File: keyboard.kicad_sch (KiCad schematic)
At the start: 352 parts, among them J1 USB_B_Micro, J2 Conn_01x06, J3 USB_C_Receptacle_USB2.0, K0 KEYSW, K1 KEYSW, K10 KEYSW, K100 KEYSW, K101 KEYSW, K102 KEYSW, K103 KEYSW, K104 KEYSW, K105 KEYSW, K106 KEYSW, K107 KEYSW, K108 KEYSW, K11 KEYSW, K12 KEYSW, K13 KEYSW, K14 KEYSW, K15 KEYSW, K16 KEYSW, K17 KEYSW, K18 KEYSW, K19 KEYSW, K2 KEYSW, K20 KEYSW, K21 KEYSW, K22 KEYSW, K23 KEYSW, K24 KEYSW, K25 KEYSW, K26 KEYSW, K27 KEYSW, K28 KEYSW, K29 KEYSW, K3 KEYSW, K30 KEYSW, K31 KEYSW, K32 KEYSW, K33 KEYSW, K34 KEYSW, K35 KEYSW, K36 KEYSW, K37 KEYSW, K38 KEYSW, K39 KEYSW, K4 KEYSW, K40 KEYSW, K41 KEYSW, K42 KEYSW, K43 KEYSW, K44 KEYSW, K45 KEYSW, K46 KEYSW, K47 KEYSW, K48 KEYSW, K49 KEYSW, K5 KEYSW, K50 KEYSW, K51 KEYSW, K52 KEYSW, K53 KEYSW, K54 KEYSW, K55 KEYSW, K56 KEYSW, K57 KEYSW, K58 KEYSW, K59 KEYSW, K6 KEYSW, K60 KEYSW, K61 KEYSW, K62 KEYSW, K63 KEYSW, K64 KEYSW, K65 KEYSW, K66 KEYSW, K67 KEYSW, K68 KEYSW, K69 KEYSW, K7 KEYSW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

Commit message: leds 1
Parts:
- renumbered D109 to D200, D123 to D201, D130 to D202, D135 to D203, D140 to D204, D148 to D205, D154 to D206, D159 to D207, D164 to D208, D171 to D209, D178 to D210, D182 to D211, D186 to D212, D199 to D213, D210 to D214, D218 to D215, D187 to D216, D195 to D217, D206 to D218, D215 to D219, D113 to D220, D118 to D221, D124 to D222, D129 to D223, D134 to D224, D139 to D225, D144 to D226, D150 to D227, D155 to D228, D160 to D229, D166 to D230, D172 to D231, D177 to D232, D184 to D233, D196 to D234, D207 to D235, D216 to D236, D188 to D237, D197 to D238, D208 to D239, D217 to D240, D115 to D241, D120 to D242, D126 to D243, D131 to D244, D136 to D245, D141 to D246, D145 to D247, D151 to D248, D156 to D249, D161 to D250, D167 to D251, D173 to D252, D179 to D253, D185 to D254, D194 to D255, D203 to D256, D214 to D257, D190 to D258, D200 to D259, D211 to D260, D219 to D261, D117 to D262, D122 to D263, D128 to D264, D133 to D265, D138 to D266, D143 to D267, D147 to D268, D153 to D269, D158 to D270, D163 to D271, D169 to D272, D175 to D273, D180 to D274

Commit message: pcb almost done
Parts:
- removed J1: USB_B_Micro, Connector_USB:USB_Micro-B_Wuerth_629105150521_CircularHoles, symbol Connector:USB_B_Micro
- added C9: 0.1u, Capacitor_SMD:C_0805_2012Metric_Pad1.15x1.40mm_HandSolder, symbol Device:C
- added F1: Fuse, Fuse:Fuse_1206_3216Metric_Pad1.42x1.75mm_HandSolder, symbol Device:Fuse
- added JP3: Jumper_2_Open, Jumper:SolderJumper-2_P1.3mm_Open_Pad1.0x1.5mm, symbol Jumper:Jumper_2_Open
- added JP4: SolderJumper_3_Open, Jumper:SolderJumper-3_P1.3mm_Open_RoundedPad1.0x1.5mm, symbol Jumper:SolderJumper_3_Open
- added Q1: Q_PMOS_DGS, Package_TO_SOT_SMD:ATPAK-2, symbol Device:Q_PMOS_DSG
- added Q2: Q_NMOS_DGS, Package_TO_SOT_SMD:SOT-23, symbol Device:Q_NMOS_DSG
- added R1, R4: 5.11k, Resistor_SMD:R_0805_2012Metric_Pad1.20x1.40mm_HandSolder, symbol Device:R
- added R5: 1M, Resistor_SMD:R_0805_2012Metric_Pad1.20x1.40mm_HandSolder, symbol Device:R
- added R6: 10k, Resistor_SMD:R_0805_2012Metric_Pad1.20x1.40mm_HandSolder, symbol Device:R
- added R7: 220k, Resistor_SMD:R_0805_2012Metric_Pad1.20x1.40mm_HandSolder, symbol Device:R
- added X1: ASE-xxxMHz, Oscillator:Oscillator_SMD_Abracon_ASE-4Pin_3.2x2.5mm, symbol Oscillator:ASE-xxxMHz
- C6, C7, C8: footprint Capacitor_SMD:C_0805_2012Metric_Pad1.15x1.40mm_HandSolder -> Capacitor_SMD:C_0805_2012Metric_Pad1.18x1.45mm_HandSolder
- J2: footprint Connector_PinHeader_2.54mm:PinHeader_1x06_P2.54mm_Vertical -> Connector_PinHeader_1.27mm:PinHeader_1x06_P1.27mm_Vertical
- J3: footprint (none) -> Connector_USB:USB_C_Receptacle_GCT_USB4085
- renumbered D189 to D275, D198 to D276, D209 to D277, D116 to D278, D121 to D279, D127 to D280, D132 to D281, D137 to D282, D142 to D283, D146 to D284, D152 to D285, D157 to D286, D162 to D287, D168 to D288, D174 to D289, D181 to D290, D205 to D291, D191 to D292, D201 to D293, D212 to D294, D220 to D295, D114 to D296, D119 to D297, D125 to D298, D149 to D299, D165 to D300, D170 to D301, D176 to D302, D183 to D303, D193 to D304, D202 to D305, D213 to D306, D192 to D307, D204 to D308
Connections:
- net Col_0: now also U1.20 (PA4); no longer U1.4 (PC15)
- net Col_1: now also U1.21 (PA5); no longer U1.3 (PC14)
- net GND: now also D110.2 (VSS), D111.2 (VSS), D112.2 (VSS), D200.2 (VSS), D201.2 (VSS), D202.2 (VSS), D203.2 (VSS), D204.2 (VSS), D205.2 (VSS), D206.2 (VSS), D207.2 (VSS), D208.2 (VSS), D209.2 (VSS), D210.2 (VSS), D211.2 (VSS), D212.2 (VSS), D213.2 (VSS), D214.2 (VSS), D215.2 (VSS), D216.2 (VSS), D217.2 (VSS), D218.2 (VSS), D219.2 (VSS), D220.2 (VSS), D221.2 (VSS), D222.2 (VSS), D223.2 (VSS), D224.2 (VSS), D225.2 (VSS), D226.2 (VSS), D227.2 (VSS), D228.2 (VSS), D229.2 (VSS), D230.2 (VSS), D231.2 (VSS), D232.2 (VSS), D233.2 (VSS), D234.2 (VSS), D235.2 (VSS), D236.2 (VSS), D237.2 (VSS), D238.2 (VSS), D239.2 (VSS), D240.2 (VSS), D241.2 (VSS), D242.2 (VSS), D243.2 (VSS), D244.2 (VSS), D245.2 (VSS), D246.2 (VSS), D247.2 (VSS), D248.2 (VSS), D249.2 (VSS), D250.2 (VSS), D251.2 (VSS), D252.2 (VSS), D253.2 (VSS), D254.2 (VSS), D255.2 (VSS), D256.2 (VSS), D257.2 (VSS), D258.2 (VSS), D259.2 (VSS), D260.2 (VSS), D261.2 (VSS), D262.2 (VSS), D263.2 (VSS), D264.2 (VSS), D265.2 (VSS), D266.2 (VSS), D267.2 (VSS), D268.2 (VSS), D269.2 (VSS), D270.2 (VSS), D271.2 (VSS), D272.2 (VSS), D273.2 (VSS), D274.2 (VSS), D275.2 (VSS), D276.2 (VSS), D277.2 (VSS), D278.2 (VSS), D279.2 (VSS), D280.2 (VSS), D281.2 (VSS), D282.2 (VSS), D283.2 (VSS), D284.2 (VSS), D285.2 (VSS), D286.2 (VSS), D287.2 (VSS), D288.2 (VSS), D289.2 (VSS), D290.2 (VSS), D291.2 (VSS), D292.2 (VSS), D293.2 (VSS), D294.2 (VSS), D295.2 (VSS), D296.2 (VSS), D297.2 (VSS), D298.2 (VSS), D299.2 (VSS), D300.2 (VSS), D301.2 (VSS), D302.2 (VSS), D303.2 (VSS), D304.2 (VSS), D305.2 (VSS), D306.2 (VSS), D307.2 (VSS), D308.2 (VSS), J3.A1 (GND), J3.A12 (GND), J3.B1 (GND), J3.B12 (GND), C9.2, JP4.3 (B), Q2.2 (S), R1.2, R4.2, R5.1, X1.2 (GND)
- net VBUS: now also J3.A4 (VBUS), J3.A9 (VBUS), J3.B4 (VBUS), J3.B9 (VBUS), F1.1
- net VCC: now also C9.1, JP4.1 (A), X1.4 (Vdd)
- net at R2.1: now also U1.44 (PA11); no longer U1.45 (PA12)
- net at R2.2: now also J3.A7 (D-), J3.B7 (D-)
- net at R3.1: now also U1.45 (PA12); no longer U1.44 (PA11)
- net at R3.2: now also J3.A6 (D+), J3.B6 (D+)
- net at D208.1 (DOUT): now also D209.3 (DIN)
- net at D208.3 (DIN): now also D207.1 (DOUT)
- net +5V: now reaches D208.4 (VDD)
- net +5V: now also D110.4 (VDD), D111.4 (VDD), D112.4 (VDD), D200.4 (VDD), D201.4 (VDD), D202.4 (VDD), D203.4 (VDD), D204.4 (VDD), D205.4 (VDD), D206.4 (VDD), D207.4 (VDD), D209.4 (VDD), D210.4 (VDD), D211.4 (VDD), D212.4 (VDD), D213.4 (VDD), D214.4 (VDD), D215.4 (VDD), D216.4 (VDD), D217.4 (VDD), D218.4 (VDD), D219.4 (VDD), D220.4 (VDD), D221.4 (VDD), D222.4 (VDD), D223.4 (VDD), D224.4 (VDD), D225.4 (VDD), D226.4 (VDD), D227.4 (VDD), D228.4 (VDD), D229.4 (VDD), D230.4 (VDD), D231.4 (VDD), D232.4 (VDD), D233.4 (VDD), D234.4 (VDD), D235.4 (VDD), D236.4 (VDD), D237.4 (VDD), D238.4 (VDD), D239.4 (VDD), D240.4 (VDD), D241.4 (VDD), D242.4 (VDD), D243.4 (VDD), D244.4 (VDD), D245.4 (VDD), D246.4 (VDD), D247.4 (VDD), D248.4 (VDD), D249.4 (VDD), D250.4 (VDD), D251.4 (VDD), D252.4 (VDD), D253.4 (VDD), D254.4 (VDD), D255.4 (VDD), D256.4 (VDD), D257.4 (VDD), D258.4 (VDD), D259.4 (VDD), D260.4 (VDD), D261.4 (VDD), D262.4 (VDD), D263.4 (VDD), D264.4 (VDD), D265.4 (VDD), D266.4 (VDD), D267.4 (VDD), D268.4 (VDD), D269.4 (VDD), D270.4 (VDD), D271.4 (VDD), D272.4 (VDD), D273.4 (VDD), D274.4 (VDD), D275.4 (VDD), D276.4 (VDD), D277.4 (VDD), D278.4 (VDD), D279.4 (VDD), D280.4 (VDD), D281.4 (VDD), D282.4 (VDD), D283.4 (VDD), D284.4 (VDD), D285.4 (VDD), D286.4 (VDD), D287.4 (VDD), D288.4 (VDD), D289.4 (VDD), D290.4 (VDD), D291.4 (VDD), D292.4 (VDD), D293.4 (VDD), D294.4 (VDD), D295.4 (VDD), D296.4 (VDD), D297.4 (VDD), D298.4 (VDD), D299.4 (VDD), D300.4 (VDD), D301.4 (VDD), D302.4 (VDD), D303.4 (VDD), D304.4 (VDD), D305.4 (VDD), D306.4 (VDD), D307.4 (VDD), D308.4 (VDD), JP3.1 (A), Q1.1 (D)
- net at D253.1 (DOUT): now also D254.3 (DIN)
- net at D253.3 (DIN): now also D252.1 (DOUT)
- net at D259.1 (DOUT): now also D260.3 (DIN)
- net at D259.3 (DIN): now also D258.1 (DOUT)
- net at D302.1 (DOUT): now also D301.3 (DIN)
- net at D302.3 (DIN): now also D303.1 (DOUT)
- net at D241.1 (DOUT): now also D242.3 (DIN)
- net at D241.3 (DIN): now also D220.1 (DOUT)
- net at D303.3 (DIN): now also D304.1 (DOUT)
- net at D256.1 (DOUT): now also D257.3 (DIN)
- net at D256.3 (DIN): now also D255.1 (DOUT)
- net at D267.1 (DOUT): now also D266.3 (DIN)
- net at D267.3 (DIN): now also D268.1 (DOUT)
- net at D301.1 (DOUT): now also D300.3 (DIN)
- net at D295.1 (DOUT): now also D308.3 (DIN)
- net at D295.3 (DIN): now also D294.1 (DOUT)
- net at D220.3 (DIN): now also D221.1 (DOUT)
- net at D299.1 (DOUT): now also D298.3 (DIN)
- net at D299.3 (DIN): now also D300.1 (DOUT)
- net at D110.1 (DOUT): now also D274.3 (DIN)
- net at D110.3 (DIN): now also D111.1 (DOUT)
- net at D269.1 (DOUT): now also D268.3 (DIN)
- net at D269.3 (DIN): now also D270.1 (DOUT)
- net at D255.3 (DIN): now also D254.1 (DOUT)
- net at D242.1 (DOUT): now also D243.3 (DIN)
- net at D262.1 (DOUT): now also D278.3 (DIN)
- net at D262.3 (DIN): now also D263.1 (DOUT)
- net at D205.1 (DOUT): now also D206.3 (DIN)
- net at D205.3 (DIN): now also D204.1 (DOUT)
- net at D280.1 (DOUT): now also D281.3 (DIN)
- net at D280.3 (DIN): now also D279.1 (DOUT)
- net at D239.1 (DOUT): now also D238.3 (DIN)
- net at D239.3 (DIN): now also D240.1 (DOUT)
- net at D305.1 (DOUT): now also D304.3 (DIN)
- net at D305.3 (DIN): now also D306.1 (DOUT)
- net at D224.1 (DOUT): now also D223.3 (DIN)
- net at D224.3 (DIN): now also D225.1 (DOUT)
- net at D237.1 (DOUT): now also D236.3 (DIN)
- net at D237.3 (DIN): now also D238.1 (DOUT)
- net at D216.1 (DOUT): now also D217.3 (DIN)
- net at D216.3 (DIN): now also D215.1 (DOUT)
- net at D229.1 (DOUT): now also D228.3 (DIN)
- net at D229.3 (DIN): now also D230.1 (DOUT)
- net at D293.1 (DOUT): now also D294.3 (DIN)
- net at D293.3 (DIN): now also D292.1 (DOUT)
- net at D289.1 (DOUT): now also D290.3 (DIN)
- net at D289.3 (DIN): now also D288.1 (DOUT)
- net at D281.1 (DOUT): now also D282.3 (DIN)
- net D_LED: now reaches U1.41 (PA8)
- net D_LED: now also D200.3 (DIN)
- net LED_EN: now reaches U1.61 (PB8)
- net LED_EN: now also R7.1
- net at D230.3 (DIN): now also D231.1 (DOUT)
- net at D286.1 (DOUT): now also D287.3 (DIN)
- net at D286.3 (DIN): now also D285.1 (DOUT)
- net at D235.1 (DOUT): now also D234.3 (DIN)
- net at D235.3 (DIN): now also D236.1 (DOUT)
- net at D243.1 (DOUT): now also D244.3 (DIN)
- net at D307.1 (DOUT): now also D306.3 (DIN)
- net at D307.3 (DIN): now also D308.1 (DOUT)
- net at D257.1 (DOUT): now also D258.3 (DIN)
- net at D225.3 (DIN): now also D226.1 (DOUT)
- net at D251.1 (DOUT): now also D252.3 (DIN)
- net at D251.3 (DIN): now also D250.1 (DOUT)
- net at D273.1 (DOUT): now also D272.3 (DIN)
- net at D273.3 (DIN): now also D274.1 (DOUT)
- net at D203.1 (DOUT): now also D204.3 (DIN)
- net at D203.3 (DIN): now also D202.1 (DOUT)
- net at D232.1 (DOUT): now also D231.3 (DIN)
- net at D232.3 (DIN): now also D233.1 (DOUT)
- net at D233.3 (DIN): now also D234.1 (DOUT)
- net at D275.1 (DOUT): now also D112.3 (DIN)
- net at D275.3 (DIN): now also D276.1 (DOUT)
- net at D284.1 (DOUT): now also D285.3 (DIN)
- net at D284.3 (DIN): now also D283.1 (DOUT)
- net at J3.A5 (CC1): now also R4.1
- net at J3.B5 (CC2): now also R1.1
- net at J3.S1 (SHIELD): now also R5.2
- net at D290.1 (DOUT): now also D291.3 (DIN)
- net at D297.1 (DOUT): now also D296.3 (DIN)
- net at D297.3 (DIN): now also D298.1 (DOUT)
- net at D282.1 (DOUT): now also D283.3 (DIN)
- net at D211.1 (DOUT): now also D212.3 (DIN)
- net at D211.3 (DIN): now also D210.1 (DOUT)
- net at D248.1 (DOUT): now also D249.3 (DIN)
- net at D248.3 (DIN): now also D247.1 (DOUT)
- net at D218.1 (DOUT): now also D219.3 (DIN)
- net at D218.3 (DIN): now also D217.1 (DOUT)
- net at D221.3 (DIN): now also D222.1 (DOUT)
- net at D201.1 (DOUT): now also D202.3 (DIN)
- net at D201.3 (DIN): now also D200.1 (DOUT)
- net at D291.1 (DOUT): now also D292.3 (DIN)
- net at D223.1 (DOUT): now also D222.3 (DIN)
- net at D215.3 (DIN): now also D214.1 (DOUT)
- net at D276.3 (DIN): now also D277.1 (DOUT)
- net at D249.1 (DOUT): now also D250.3 (DIN)
- net at D288.3 (DIN): now also D287.1 (DOUT)
- net at D213.1 (DOUT): now also D214.3 (DIN)
- net at D213.3 (DIN): now also D212.1 (DOUT)
- net at D226.3 (DIN): now also D227.1 (DOUT)
- net at D272.1 (DOUT): now also D271.3 (DIN)
- net at D111.3 (DIN): now also D112.1 (DOUT)
- net at D264.1 (DOUT): now also D263.3 (DIN)
- net at D264.3 (DIN): now also D265.1 (DOUT)
- net at D266.1 (DOUT): now also D265.3 (DIN)
- net at D207.3 (DIN): now also D206.1 (DOUT)
- net at D260.1 (DOUT): now also D261.3 (DIN)
- net at D247.3 (DIN): now also D246.1 (DOUT)
- net at D227.3 (DIN): now also D228.1 (DOUT)
- net at D240.3 (DIN): now also D219.1 (DOUT)
- net at D209.1 (DOUT): now also D210.3 (DIN)
- net at D279.3 (DIN): now also D278.1 (DOUT)
- net at D245.1 (DOUT): now also D246.3 (DIN)
- net at D245.3 (DIN): now also D244.1 (DOUT)
- net at D261.1 (DOUT): now also D277.3 (DIN)
- net at D270.3 (DIN): now also D271.1 (DOUT)
- new net: Q1.3 (G), Q2.1 (D), R6.1
- new net: JP4.2 (C), X1.1 (EN)
- new net: U1.3 (PC14), X1.3 (OUT)
- new net: Q2.3 (G), R7.2
- new net Vfuse: F1.2, JP3.2 (B), Q1.2 (S), R6.2
- no-connect marks 1 -> 3
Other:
- moved on the sheet: C1, C2, C3, C4, C5, C6, C7, C8, D110, D111, D112, D200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

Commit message: PCB finished
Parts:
- added C10, C11, C12, C13, C14, C15, C16, C17, C18, C19, C20, C21: 0.1u, Capacitor_SMD:C_0805_2012Metric_Pad1.18x1.45mm_HandSolder, symbol Device:C
- C9: footprint Capacitor_SMD:C_0805_2012Metric_Pad1.15x1.40mm_HandSolder -> Capacitor_SMD:C_0805_2012Metric_Pad1.18x1.45mm_HandSolder
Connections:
- net +5V: now also C10.1, C11.1, C12.1, C13.1, C14.1, C15.1, C16.1, C17.1, C18.1, C19.1, C20.1, C21.1
- net GND: now also C10.2, C11.2, C12.2, C13.2, C14.2, C15.2, C16.2, C17.2, C18.2, C19.2, C20.2, C21.2

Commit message: PCB finished 2
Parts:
- added DRA1: DIN_Rail_Adapter, keyboard_stabilizers:Stabilizer_Cherry_MX_6.25u, symbol Mechanical:DIN_Rail_Adapter
- added DRA2, DRA3, DRA4, DRA5, DRA6, DRA7, DRA8: DIN_Rail_Adapter, keyboard_stabilizers:Stabilizer_Cherry_MX_2.00u, symbol Mechanical:DIN_Rail_Adapter
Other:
- note added: "Stabilizers"
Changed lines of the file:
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@@
     (stroke (width 0) (type default) (color 0 0 0 0))
   )
+  (polyline (pts (xy 635 205.74) (xy 635 184.15))
+    (stroke (width 0) (type default) (color 0 0 0 0))
+  )
   (wire (pts (xy 129.54 165.1) (xy 129.54 172.72))
     (stroke (width 0) (type default) (color 0 0 0 0))
@@
     (stroke (width 0) (type default) (color 0 0 0 0))
   )
+  (polyline (pts (xy 441.96 184.15) (xy 441.96 205.74))
+    (stroke (width 0) (type default) (color 0 0 0 0))
+  )
   (wire (pts (xy 118.11 193.04) (xy 118.11 195.58))
     (stroke (width 0) (type default) (color 0 0 0 0))
@@
     (stroke (width 0) (type default) (color 0 0 0 0))
   )
+  (polyline (pts (xy 635 184.15) (xy 635 184.15))
+    (stroke (width 0) (type default) (color 0 0 0 0))
+  )
   (wire (pts (xy 52.07 160.02) (xy 52.07 158.75))
     (stroke (width 0) (type default) (color 0 0 0 0))
@@
     (stroke (width 0) (type default) (color 0 0 0 0))
   )
+  (polyline (pts (xy 441.96 205.74) (xy 635 205.74))
+    (stroke (width 0) (type default) (color 0 0 0 0))
+  )
   (wire (pts (xy 528.32 157.48) (xy 539.75 157.48))
     (stroke (width 0) (type default) (color 0 0 0 0))
@@
     (stroke (width 0) (type default) (color 0 0 0 0))
   )
+  (polyline (pts (xy 635 184.15) (xy 441.96 184.15))
+    (stroke (width 0) (type default) (color 0 0 0 0))
+  )
   (wire (pts (xy 43.18 151.13) (xy 45.72 151.13))
     (stroke (width 0) (type default) (color 0 0 0 0))
@@
     (stroke (width 0) (type default) (color 0 0 0 0))
   )
+  (text "Stabilizers" (at 443.23 186.69 0)
+    (effects (font (size 1.27 1.27)) (justify left bottom))
+  )
   (label "Row_2" (at 364.49 166.37 0)
     (effects (font (size 1.27 1.27)) (justify left bottom))
@@
     (pin "1")
   )
+  (symbol (lib_id "Mechanical:DIN_Rail_Adapter") (at 571.5 195.58 0) (unit 1)
+    (in_bom yes) (on_board yes) (fields_autoplaced)
+    (property "Reference" "DRA6" (id 0) (at 571.5 190.5 0))
+    (property "Value" "DIN_Rail_Adapter" (id 1) (at 571.5 190.5 0)
+      (effects (font (size 1.27 1.27)) hide)
+    )
+    (property "Footprint" "keyboard_stabilizers:Stabilizer_Cherry_MX_2.00u" (id 2) (at 571.5 200.66 0)
+      (effects (font (size 1.27 1.27)) hide)
+    )
+    (property "Datasheet" "~" (id 3) (at 571.5 191.77 0)
+      (effects (font (size 1.27 1.27)) hide)
+    )
+  )
   (symbol (lib_id "power:GND") (at 115.57 156.21 90) (mirror x) (unit 1)
     (in_bom yes) (on_board yes)
@@
     (pin "1")
   )
+  (symbol (lib_id "Mechanical:DIN_Rail_Adapter") (at 548.64 195.58 0) (unit 1)
+    (in_bom yes) (on_board yes) (fields_autoplaced)
+    (property "Reference" "DRA5" (id 0) (at 548.64 190.5 0))
+    (property "Value" "DIN_Rail_Adapter" (id 1) (at 548.64 190.5 0)
+      (effects (font (size 1.27 1.27)) hide)
+    )
+    (property "Footprint" "keyboard_stabilizers:Stabilizer_Cherry_MX_2.00u" (id 2) (at 548.64 200.66 0)
+      (effects (font (size 1.27 1.27)) hide)
+    )
+    (property "Datasheet" "~" (id 3) (at 548.64 191.77 0)
+      (effects (font (size 1.27 1.27)) hide)
+    )
+  )
   (symbol (lib_id "Switch:SW_Push") (at 78.74 60.96 0) (unit 1)
     (in_bom yes) (on_board yes)
@@
     (pin "1")
   )
+  (symbol (lib_id "Mechanical:DIN_Rail_Adapter") (at 502.92 195.58 0) (unit 1)
+    (in_bom yes) (on_board yes) (fields_autoplaced)
+    (property "Reference" "DRA3" (id 0) (at 502.92 190.5 0))
+    (property "Value" "DIN_Rail_Adapter" (id 1) (at 502.92 190.5 0)
+      (effects (font (size 1.27 1.27)) hide)
+    )
+    (property "Footprint" "keyboard_stabilizers:Stabilizer_Cherry_MX_2.00u" (id 2) (at 502.92 200.66 0)
+      (effects (font (size 1.27 1.27)) hide)
+    )
+    (property "Datasheet" "~" (id 3) (at 502.92 191.77 0)
+      (effects (font (size 1.27 1.27)) hide)
+    )
+  )
   (symbol (lib_id "power:+5V") (at 527.05 97.79 0) (unit 1)
     (in_bom yes) (on_board yes)
@@
     (pin "4")
   )
+  (symbol (lib_id "Mechanical:DIN_Rail_Adapter") (at 457.2 195.58 0) (unit 1)
+    (in_bom yes) (on_board yes) (fields_autoplaced)
+    (property "Reference" "DRA1" (id 0) (at 457.2 190.5 0))
+    (property "Value" "DIN_Rail_Adapter" (id 1) (at 457.2 190.5 0)
+      (effects (font (size 1.27 1.27)) hide)
+    )
+    (property "Footprint" "keyboard_stabilizers:Stabilizer_Cherry_MX_6.25u" (id 2) (at 457.2 200.66 0)
+      (effects (font (size 1.27 1.27)) hide)
+    )
+    (property "Datasheet" "~" (id 3) (at 457.2 191.77 0)
+      (effects (font (size 1.27 1.27)) hide)
+    )
+  )
+  (symbol (lib_id "Mechanical:DIN_Rail_Adapter") (at 617.22 195.58 0) (unit 1)
+    (in_bom yes) (on_board yes) (fields_autoplaced)
+    (property "Reference" "DRA8" (id 0) (at 617.22 190.5 0))
+    (property "Value" "DIN_Rail_Adapter" (id 1) (at 617.22 190.5 0)
+      (effects (font (size 1.27 1.27)) hide)
+    )
+    (property "Footprint" "keyboard_stabilizers:Stabilizer_Cherry_MX_2.00u" (id 2) (at 617.22 200.66 0)
+      (effects (font (size 1.27 1.27)) hide)
+    )
+    (property "Datasheet" "~" (id 3) (at 617.22 191.77 0)
+      (effects (font (size 1.27 1.27)) hide)
+    )
+  )
   (symbol (lib_id "power:GND") (at 746.76 69.85 0) (unit 1)
     (in_bom yes) (on_board yes)
@@
     (pin "2")
   )
+  (symbol (lib_id "Mechanical:DIN_Rail_Adapter") (at 594.36 195.58 0) (unit 1)
+    (in_bom yes) (on_board yes) (fields_autoplaced)
+    (property "Reference" "DRA7" (id 0) (at 594.36 190.5 0))
+    (property "Value" "DIN_Rail_Adapter" (id 1) (at 594.36 190.5 0)
+      (effects (font (size 1.27 1.27)) hide)
+    )
+    (property "Footprint" "keyboard_stabilizers:Stabilizer_Cherry_MX_2.00u" (id 2) (at 594.36 200.66 0)
+      (effects (font (size 1.27 1.27)) hide)
+    )
+    (property "Datasheet" "~" (id 3) (at 594.36 191.77 0)
+      (effects (font (size 1.27 1.27)) hide)
+    )
+  )
   (symbol (lib_id "power:+5V") (at 648.97 97.79 0) (unit 1)
     (in_bom yes) (on_board yes)
@@
     (pin "1")
   )
+  (symbol (lib_id "Mechanical:DIN_Rail_Adapter") (at 525.78 195.58 0) (unit 1)
+    (in_bom yes) (on_board yes) (fields_autoplaced)
+    (property "Reference" "DRA4" (id 0) (at 525.78 190.5 0))
+    (property "Value" "DIN_Rail_Adapter" (id 1) (at 525.78 190.5 0)
+      (effects (font (size 1.27 1.27)) hide)
+    )
+    (property "Footprint" "keyboard_stabilizers:Stabilizer_Cherry_MX_2.00u" (id 2) (at 525.78 200.66 0)
+      (effects (font (size 1.27 1.27)) hide)
+    )
+    (property "Datasheet" "~" (id 3) (at 525.78 191.77 0)
+      (effects (font (size 1.27 1.27)) hide)
+    )
+  )
   (symbol (lib_id "LED:SK6812MINI") (at 527.05 62.23 0) (unit 1)
     (in_bom yes) (on_board yes)
@@
     (pin "1")
   )
+  (symbol (lib_id "Mechanical:DIN_Rail_Adapter") (at 480.06 195.58 0) (unit 1)
+    (in_bom yes) (on_board yes) (fields_autoplaced)
+    (property "Reference" "DRA2" (id 0) (at 480.06 190.5 0))
+    (property "Value" "DIN_Rail_Adapter" (id 1) (at 480.06 190.5 0)
+      (effects (font (size 1.27 1.27)) hide)
+    )
+    (property "Footprint" "keyboard_stabilizers:Stabilizer_Cherry_MX_2.00u" (id 2) (at 480.06 200.66 0)
+      (effects (font (size 1.27 1.27)) hide)
+    )
+    (property "Datasheet" "~" (id 3) (at 480.06 191.77 0)
+      (effects (font (size 1.27 1.27)) hide)
+    )
+  )
   (symbol (lib_id "power:+5V") (at 567.69 97.79 0) (unit 1)
     (in_bom yes) (on_board yes)
@@
       (reference "D308") (unit 1) (value "SK6812MINI") (footprint "specialParts:SK6812-MINI-E")
     )
+    (path "/a6f96558-3526-4495-8cb8-705c7b5eea1a"
+      (reference "DRA1") (unit 1) (value "DIN_Rail_Adapter") (footprint "keyboard_stabilizers:Stabilizer_Cherry_MX_6.25u")
+    )
+    (path "/d449f57e-41c1-4ba3-a3b4-4246bda47477"
+      (reference "DRA2") (unit 1) (value "DIN_Rail_Adapter") (footprint "keyboard_stabilizers:Stabilizer_Cherry_MX_2.00u")
+    )
+    (path "/986833ae-64c8-4af6-b083-b60e216807f0"
+      (reference "DRA3") (unit 1) (value "DIN_Rail_Adapter") (footprint "keyboard_stabilizers:Stabilizer_Cherry_MX_2.00u")
+    )
+    (path "/c5953a9f-9d10-409f-b4f1-88981834ff1b"
+      (reference "DRA4") (unit 1) (value "DIN_Rail_Adapter") (footprint "keyboard_stabilizers:Stabilizer_Cherry_MX_2.00u")
+    )
+    (path "/71045c42-4b09-48fd-976a-190e01ac759f"
+      (reference "DRA5") (unit 1) (value "DIN_Rail_Adapter") (footprint "keyboard_stabilizers:Stabilizer_Cherry_MX_2.00u")
+    )
+    (path "/1640a7e2-1419-42ed-8695-c34a2bf254fe"
+      (reference "DRA6") (unit 1) (value "DIN_Rail_Adapter") (footprint "keyboard_stabilizers:Stabilizer_Cherry_MX_2.00u")
+    )
+    (path "/c413d3bb-3433-4e13-990e-3b9c0c009acf"
+      (reference "DRA7") (unit 1) (value "DIN_Rail_Adapter") (footprint "keyboard_stabilizers:Stabilizer_Cherry_MX_2.00u")
+    )
+    (path "/a710bcf7-cc50-4a33-982e-843e2d1c330f"
+      (reference "DRA8") (unit 1) (value "DIN_Rail_Adapter") (footprint "keyboard_stabilizers:Stabilizer_Cherry_MX_2.00u")
+    )
     (path "/5c9def6d-16af-4019-af0e-b4e97674c3e1"

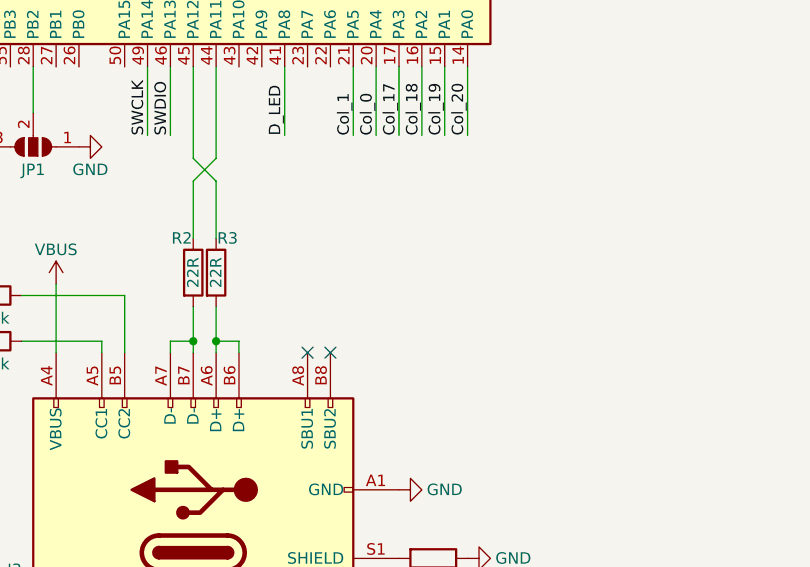
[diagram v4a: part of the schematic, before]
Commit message: Added USB cable connector
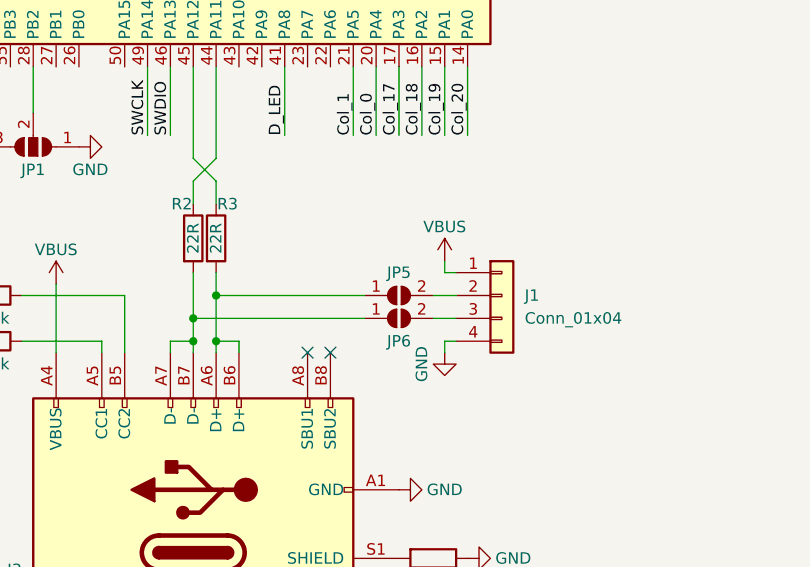
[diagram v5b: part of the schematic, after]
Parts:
- added J1: Conn_01x04, Connector_PinHeader_2.54mm:PinHeader_1x04_P2.54mm_Vertical, symbol Connector_Generic:Conn_01x04
- added JP5, JP6: SolderJumper_2_Open, Jumper:SolderJumper-2_P1.3mm_Open_RoundedPad1.0x1.5mm, symbol Jumper:SolderJumper_2_Open
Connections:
- net GND: now also J1.4 (Pin_4)
- net VBUS: now also J1.1 (Pin_1)
- net at J3.A7 (D-), J3.B7 (D-), R2.2: now also JP6.1 (A)
- net at J3.A6 (D+), J3.B6 (D+), R3.2: now also JP5.1 (A)
- new net: J1.2 (Pin_2), JP5.2 (B)
- new net: J1.3 (Pin_3), JP6.2 (B)
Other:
- moved on the sheet: R2, R3
